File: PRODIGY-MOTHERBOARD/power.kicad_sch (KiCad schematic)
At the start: 49 parts, among them J5 Barrel_Jack_MountingPin, U1 TPS22810DRV, U2 TPS54331DR, U3 TPS54331DR

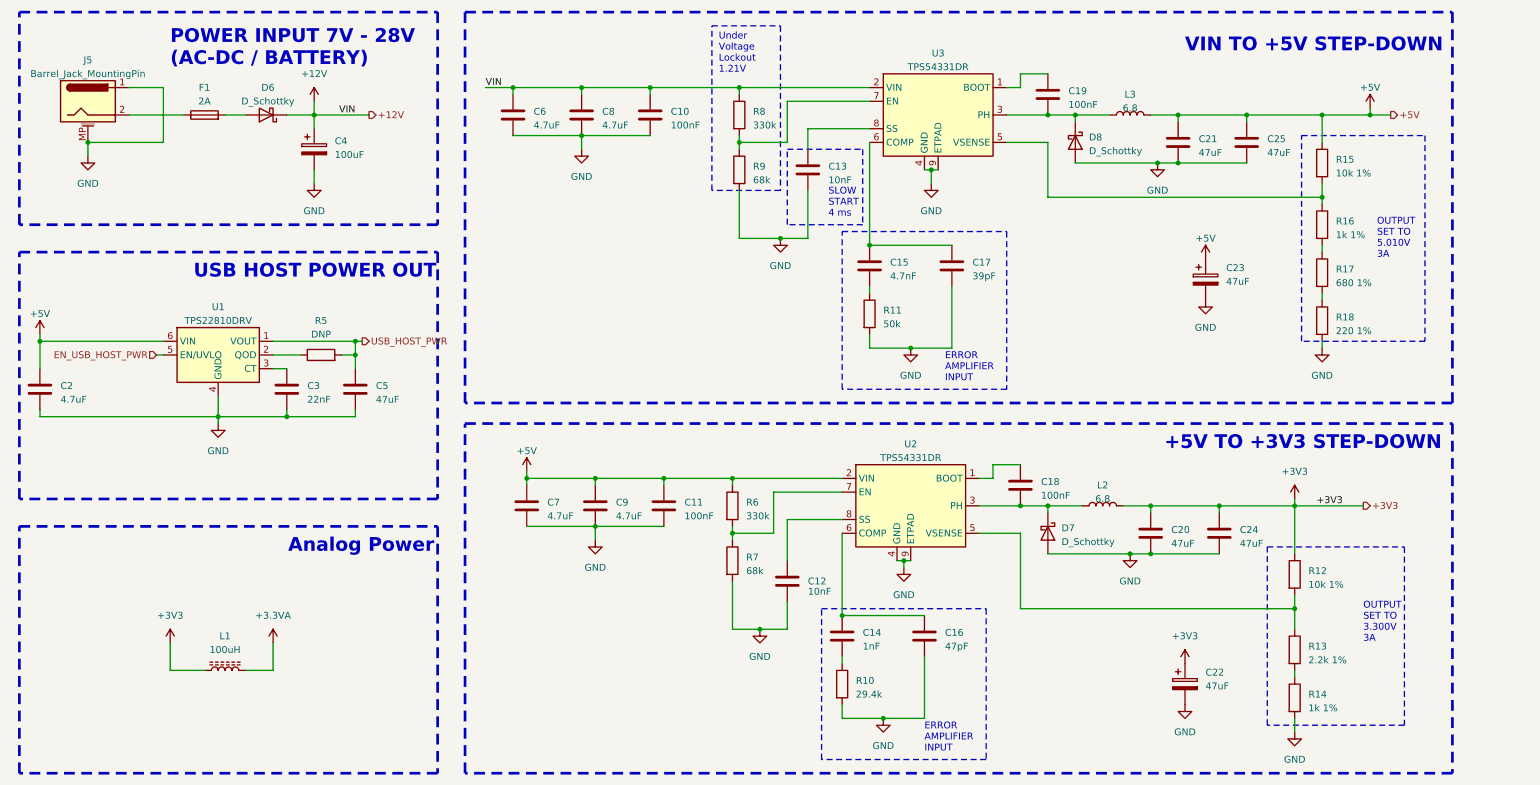
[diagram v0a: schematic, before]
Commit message: MBT Schematic improved
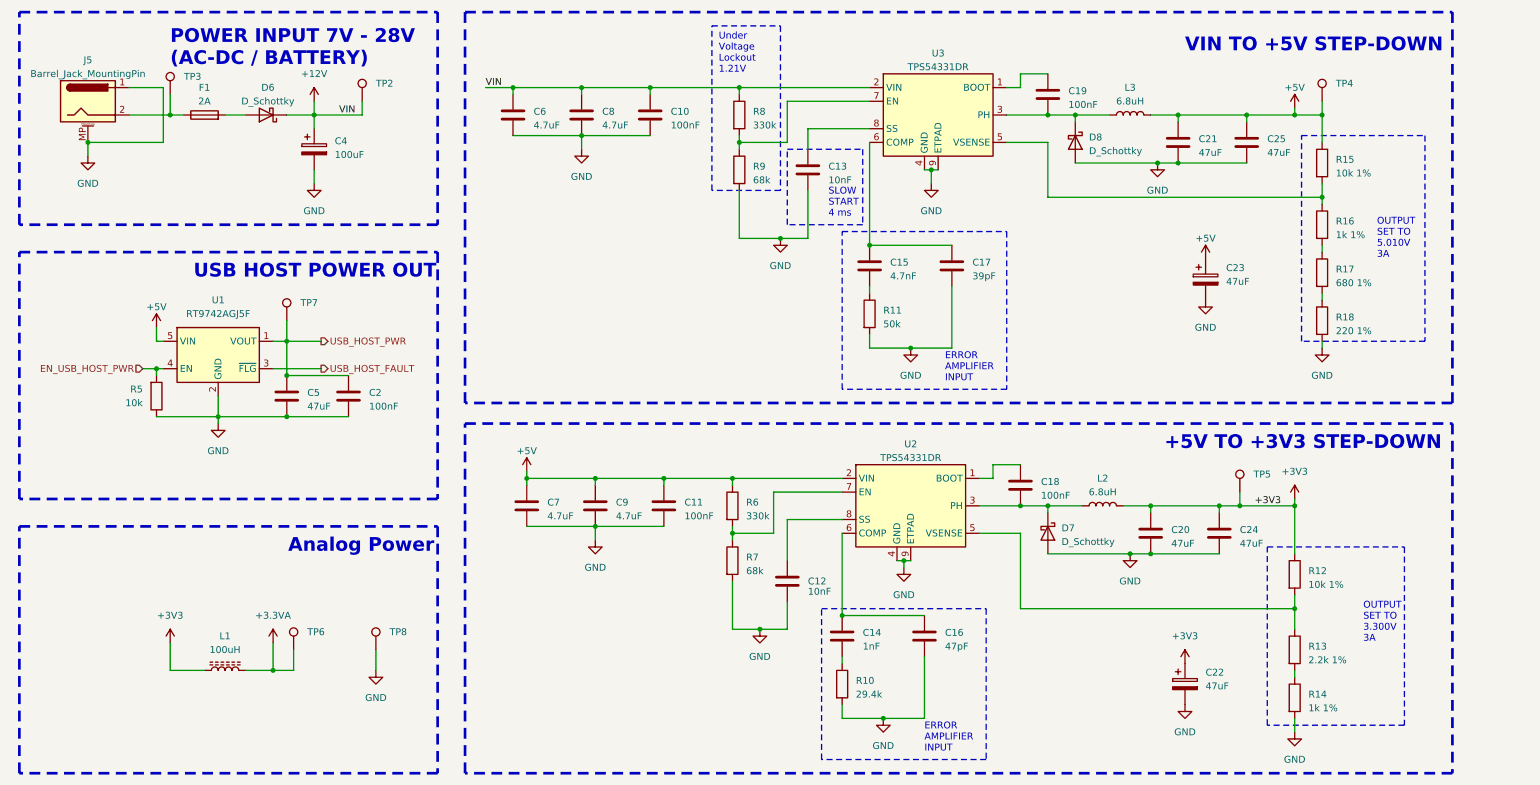
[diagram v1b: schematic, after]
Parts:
- removed C3: 22nF, Capacitor_SMD:C_0603_1608Metric, symbol Device:C
- removed U1: TPS22810DRV, Package_SON:WSON-6-1EP_2x2mm_P0.65mm_EP1x1.6mm, symbol Power_Management:TPS22810DRV
- added TP2, TP3, TP4, TP5, TP6, TP7, TP8: ~, TestPoint:TestPoint_Pad_D3.0mm, symbol Connector:TestPoint
- added U1: RT9742AGJ5F, Package_TO_SOT_SMD:TSOT-23-5, symbol Power_Management:RT9742AGJ5F
- C2: value 4.7uF -> 100nF; footprint Capacitor_SMD:C_1206_3216Metric -> Capacitor_SMD:C_0603_1608Metric
- L2, L3: value 6.8 -> 6.8uH
- R5: value DNP -> 10k
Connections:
- net +12V: now also TP2.1
- net +3.3VA: now also TP6.1
- net +3V3: now also TP5.1
- net +5V: now also TP4.1, U1.5 (VIN); no longer C2.1
- net EN_USB_HOST_PWR: now also R5.2, U1.4 (EN)
- net GND: now also R5.1, TP8.1, U1.2 (GND)
- net USB_HOST_PWR: now also C2.1, TP7.1, U1.1 (VOUT); no longer R5.2
- net at F1.1, J5.2: now also TP3.1
- new net USB_HOST_FAULT: U1.3 (~{FLG})
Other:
- moved on the sheet: C5

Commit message: schematic v0.2 finalized
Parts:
- renumbered C11 to C10, C12 to C11, C13 to C12, C14 to C13, C15 to C14, C16 to C15, C17 to C16, C18 to C17, C19 to C18, C20 to C19, C5 to C2, C21 to C20, C22 to C21, C23 to C22, C24 to C23, C25 to C24, C4 to C3, C2 to C4, C6 to C5, C7 to C6, C8 to C7, C9 to C8, C10 to C9, TP3 to TP2, TP7 to TP3, TP6 to TP4, TP2 to TP5, TP8 to TP6, TP5 to TP7, TP4 to TP8

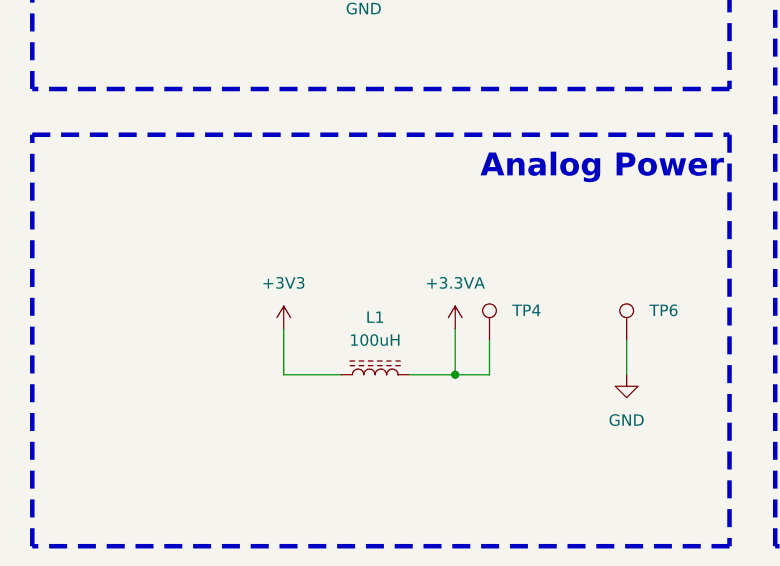
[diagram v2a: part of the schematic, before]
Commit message: Motherboard footprints assigned.
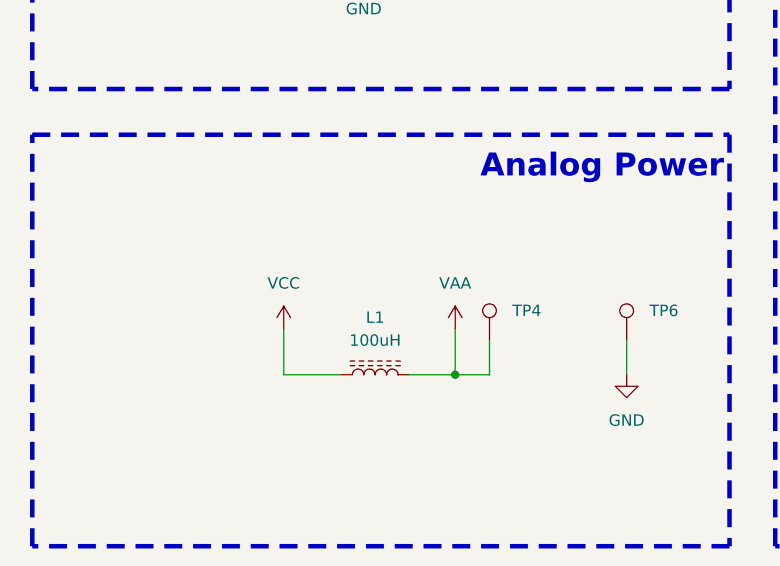
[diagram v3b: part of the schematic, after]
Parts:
- C21, C22: footprint Capacitor_SMD:CP_Elec_6.3x5.8 -> Capacitor_SMD:C_1210_3225Metric
- C5, C6, C7, C8: footprint Capacitor_SMD:C_1206_3216Metric -> Capacitor_SMD:C_0805_2012Metric
- L1: footprint (none) -> Inductor_SMD:L_0805_2012Metric
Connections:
- net +3V3: no longer L1.1
- net +3.3VA renamed VAA
- new net VCC: L1.1

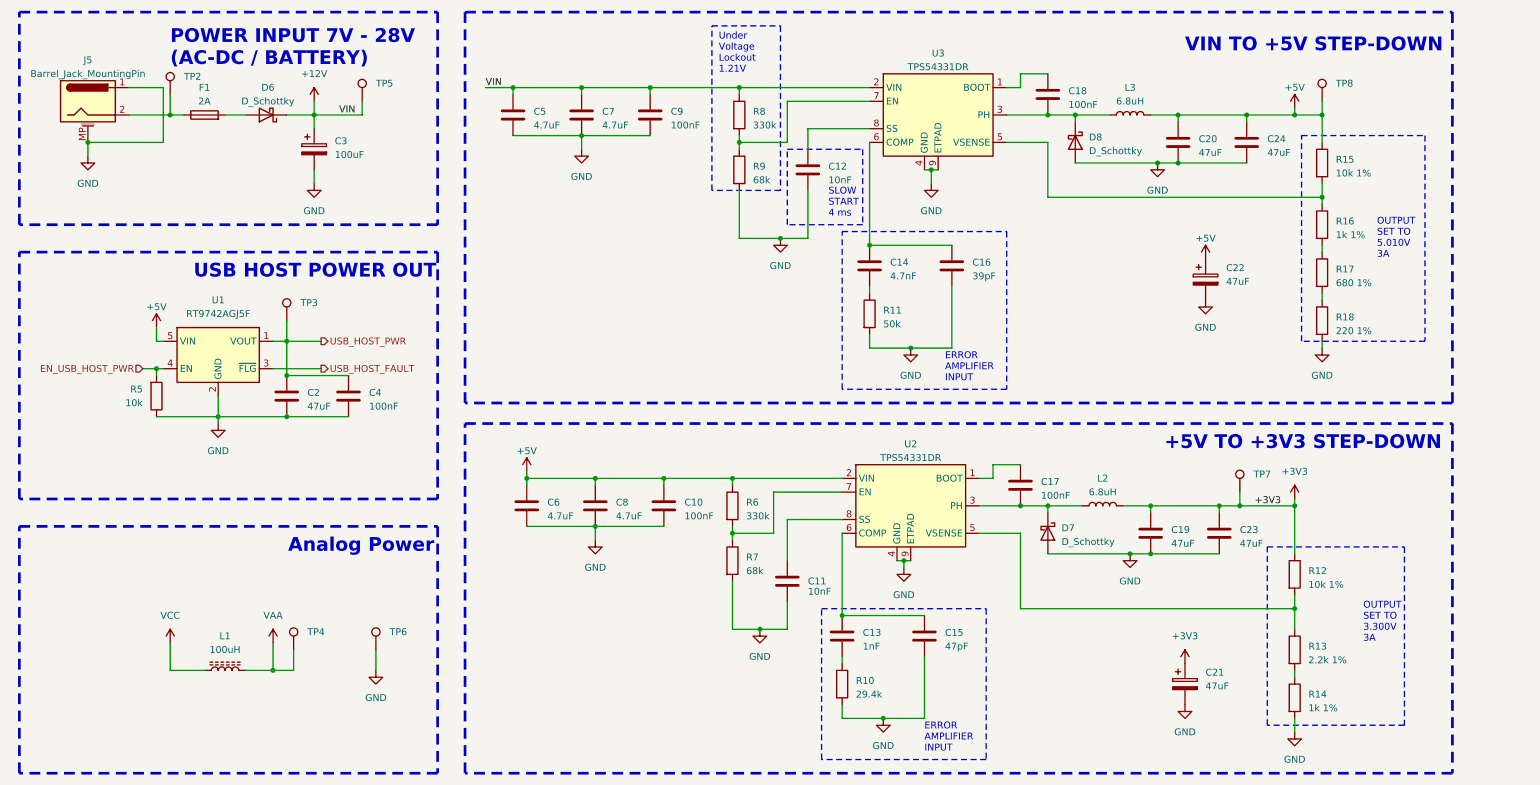
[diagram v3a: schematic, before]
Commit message: finished motherboard bom and updated footprints
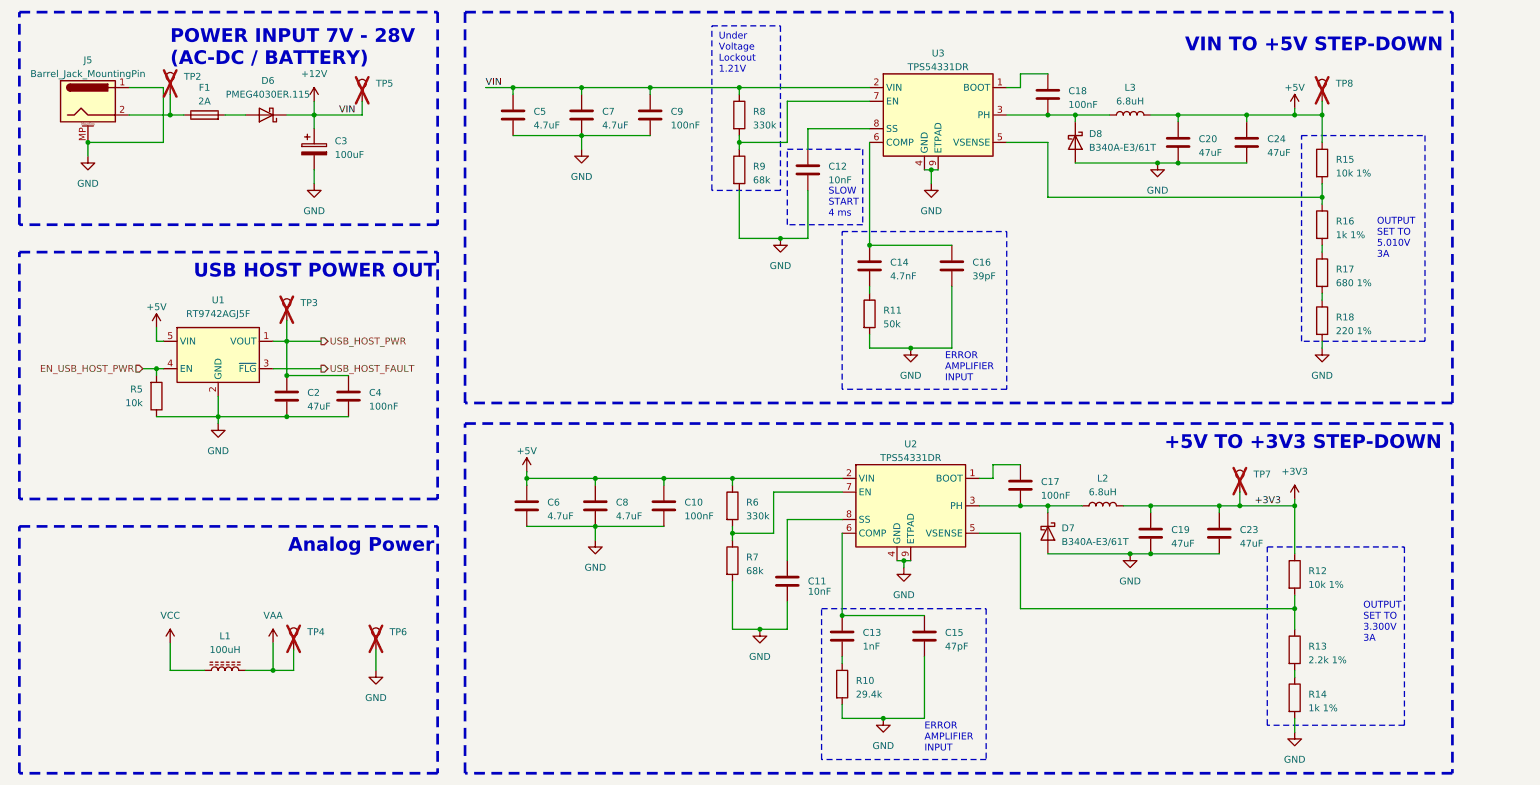
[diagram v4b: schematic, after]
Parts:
- removed C21, C22: 47uF, Capacitor_SMD:C_1210_3225Metric, symbol Device:C_Polarized
- C10, C17, C18, C4, C9: TME (none) -> CL10B104KB8NNNC
- C11, C12: TME (none) -> 06035C103JAT2A
- C13: TME (none) -> 0603B102K500CT
- C14: TME (none) -> 06031C472KAT2A
- C15: TME (none) -> 06035A470JAT2A
- C16: TME (none) -> 06035A390JAT2A
- C19, C2, C20, C23, C24: TME (none) -> GRM32ER61C476KE15L
- C3: TME (none) -> EEEFPV101XAP
- C5, C6, C7, C8: TME (none) -> CL21A475KAQNNNG
- D6: value D_Schottky -> PMEG4030ER.115; footprint Diode_SMD:D_SMB -> Diode_SMD:Nexperia_CFP3_SOD-123W; TME (none) -> PMEG4030ER.115
- D7, D8: value D_Schottky -> B340A-E3/61T; footprint Diode_SMD:D_SMB -> Diode_SMD:D_SMA; TME (none) -> B340A-E3/61T
- F1: footprint Fuse:Fuse_1206_3216Metric -> Fuse:Fuse_1812_4532Metric; TME (none) -> 0ZCF0200AF2C
- J5: footprint Connector_BarrelJack:BarrelJack_CUI_PJ-063AH_Horizontal -> Connector_BarrelJack:BarrelJack_Horizontal; TME (none) -> FC68148
- L1: footprint Inductor_SMD:L_0805_2012Metric -> Inductor_SMD:L_1210_3225Metric; TME (none) -> NLCV32T-101K-EF
- L2, L3: TME (none) -> HPI0630-6R8
- R10: TME (none) -> ERJ3EKF3302V
- R11: TME (none) -> AR0603-50K-0.1%
- R12, R15, R5: TME (none) -> WR06X1002FTL
- R13: TME (none) -> AC0603FR-072K2L
- R14, R16: TME (none) -> RC0603JR-071K
- R17: TME (none) -> ERJ3EKF6800V
- R18: TME (none) -> ERJ3EKF2200V
- R6, R8: TME (none) -> ERJ3EKF3303V
- R7, R9: TME (none) -> ERJ3EKF6802V
- TP2, TP3, TP4, TP5, TP6, TP7, TP8: now not fitted
- U1: MOUSER (none) -> 835-RT9742AGJ5F
- U2, U3: TME (none) -> TPS54331DR

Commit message: v0.1.1 schematic and pcb updated. gerbers exported, ready for production
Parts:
- removed U2, U3: TPS54331DR, Package_SO:TI_SO-PowerPAD-8_ThermalVias, symbol Regulator_Switching:TPS54336ADDA
- added U2, U3: TPS54331DR, Package_SO:TI_SO-PowerPAD-8_ThermalVias, symbol 0_TPS5433:TPS54331DR
- F1: footprint Fuse:Fuse_1812_4532Metric -> Fuse:Fuse_2920_7451Metric
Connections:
- net +12V: now also C10.1, C6.1, C8.1, R6.1, U2.2 (VIN), U3.2 (VIN)
- net +5V: no longer C10.1, C6.1, C8.1, R6.1
- net GND: now also J5.2, U2.7 (GND), U2.9 (ETPAD), U3.7 (GND), U3.9 (ETPAD); no longer J5.1
- net at F1.1, TP2.1: now also J5.1; no longer J5.2
- net at C14.1, C16.1: now also U3.6 (COMP)
- net at C17.1: now also U2.1 (BOOT)
- net at C17.2, D7.1 (K), L2.1: now also U2.8 (PH)
- net at R12.2, R13.1: now also U2.5 (VSENSE)
- net at C13.1, C15.1: now also U2.6 (COMP)
- net at R6.2, R7.1: now also U2.3 (EN)
- net at C11.1: now also U2.4 (SS)
- net at R15.2, R16.1: now also U3.5 (VSENSE)
- net at C18.2, D8.1 (K), L3.1: now also U3.8 (PH)
- net at R8.2, R9.1: now also U3.3 (EN)
- net at C12.1: now also U3.4 (SS)
- net at C18.1: now also U3.1 (BOOT)
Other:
- note added: "NOTE: Power Input Corrected orientation of Barrel jack. Corrected footprint of the fuse."
- note added: "NOTE: Power rail sourcing 3V3 regulator is sourced from 12V instead of 5V"
- note added: "NOTE: Resistor feedback network Alternatively use: R13 - 3.24k 1% R14 - 0R"
- note added: "NOTE: Resistor feedback network Alternatively use: R16 - 1.91k R17 - 0R R18 - 0R"
- note added: "NOTE: TPS54331DR Symbol Corrected the component's pinout."
- moved on the sheet: J5
